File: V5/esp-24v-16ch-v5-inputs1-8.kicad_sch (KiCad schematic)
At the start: 10 parts, among them U9 OR-3H7-4

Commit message: Many changes!
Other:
- note added: "RESISTORS: 62,5mW WHERE NOT SPECIFIED"
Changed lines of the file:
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@@
+		)
+	)
+	(text "RESISTORS: 62,5mW WHERE NOT SPECIFIED"
+		(exclude_from_sim no)
+		(at 181.61 173.99 0)
+		(effects
+			(font
+				(size 1.905 1.905)
+			)
+			(justify left)
 		)
 	)

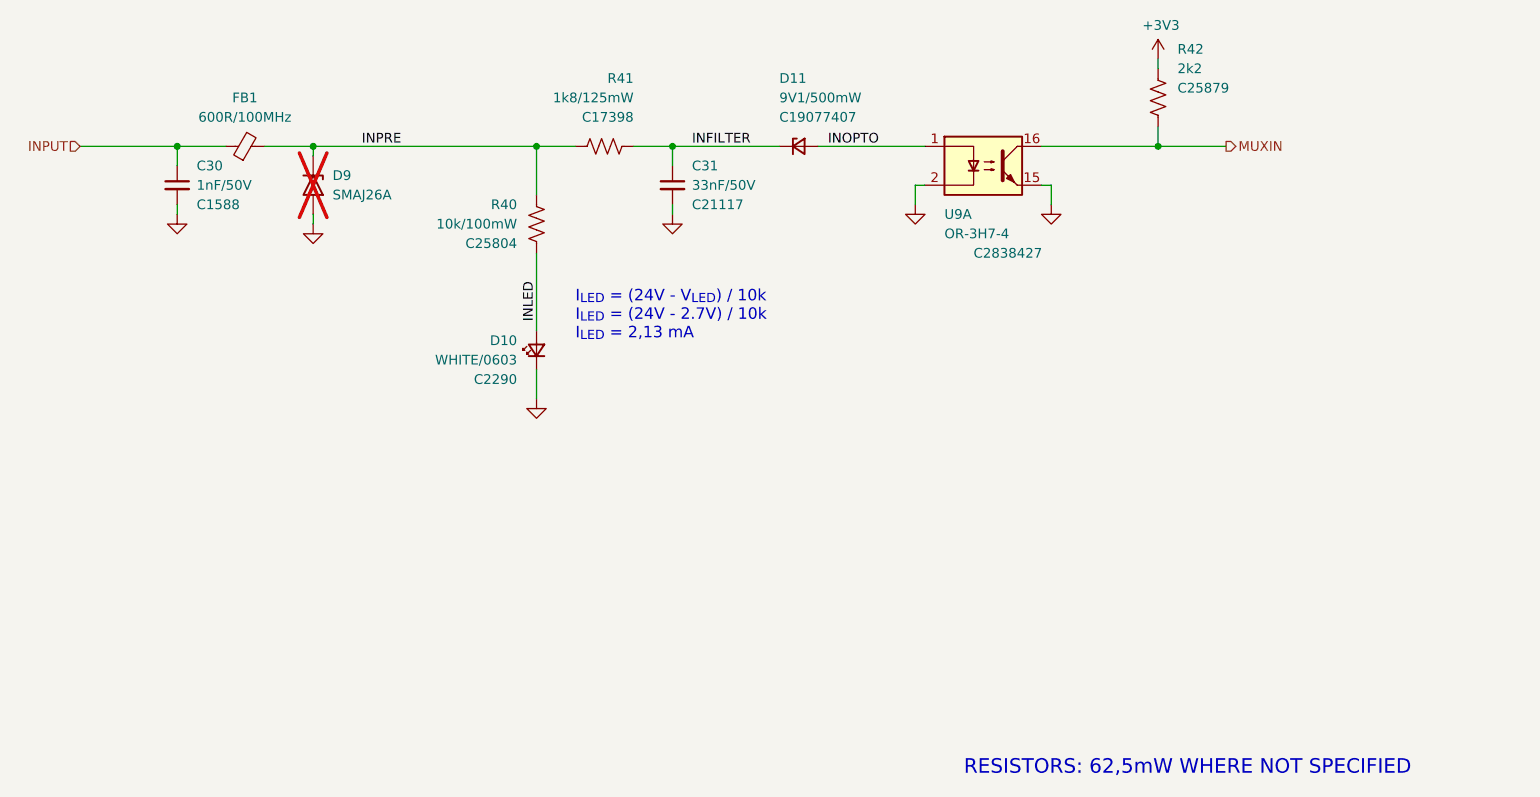
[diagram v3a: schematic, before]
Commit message: Inputs GND separated from main GND.
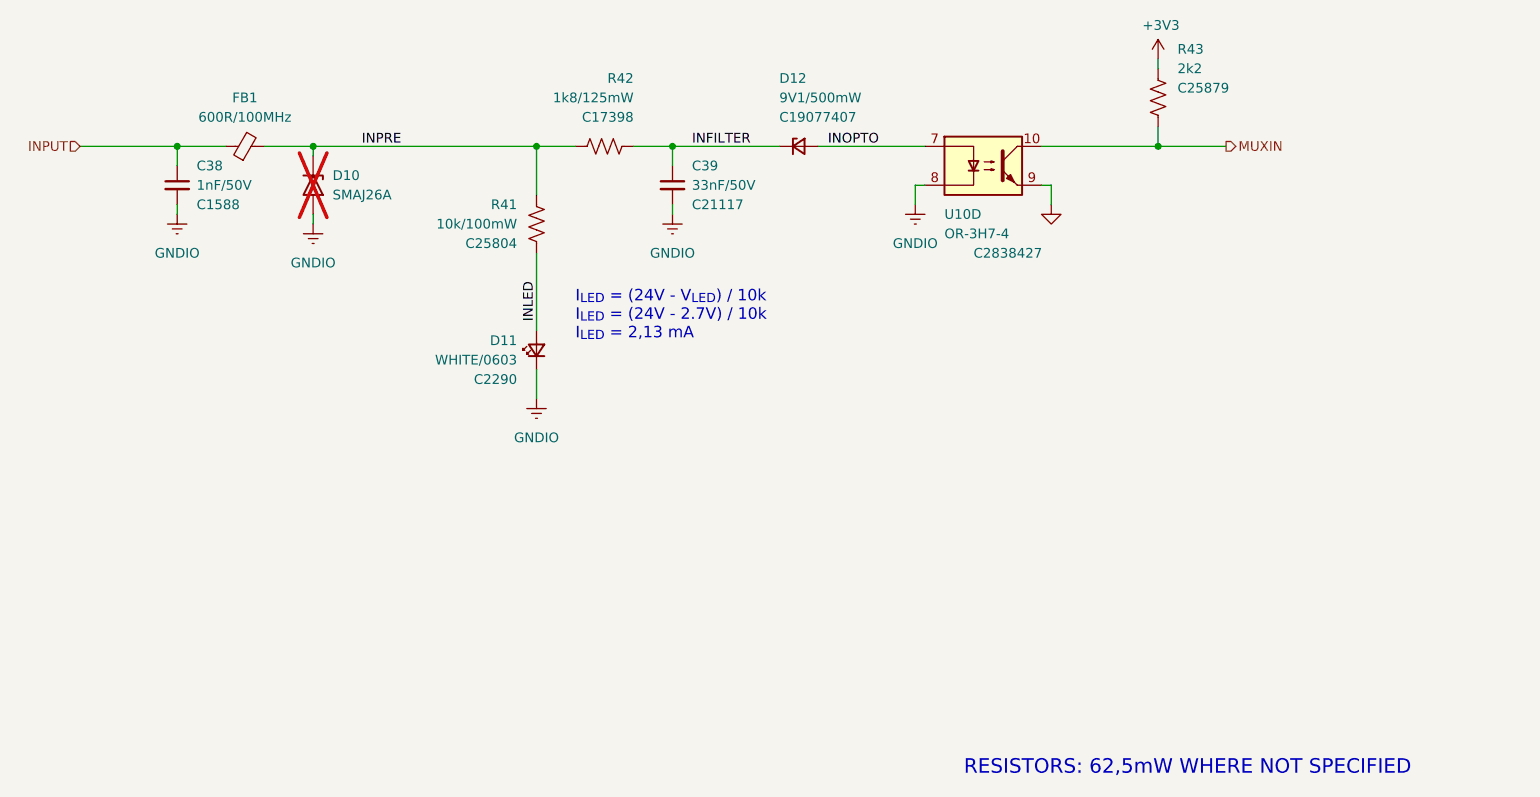
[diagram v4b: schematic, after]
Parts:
- renumbered C30 to C38, C31 to C39, D9 to D10, D10 to D11, D11 to D12, R40 to R41, R41 to R42, R42 to R43, U9 to U10
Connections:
- net GND: now also U10.9; no longer C38.2, C39.2, D10.2 (A2), D11.1 (K), U10.15, U10.2
- net INOPTO: now also U10.7; no longer U10.1
- net MUXIN: now also U10.10; no longer U10.16
- new net GNDIO: C38.2, C39.2, D10.2 (A2), D11.1 (K), U10.8
